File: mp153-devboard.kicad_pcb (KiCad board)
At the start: 4 copper layers, 39.9 x 57.9 mm, 117 parts, among them CON1 microSDCon_SMT_104031-0811, J1 Pins_02x04_RightAngle_P2.54mm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, J2 Pins_02x05_P1.27mm_SMT, J3 USB-C_Receptacle_Molex_217179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, J4 Pins_02x40_P0.4mm_W3.0mm_SMT, J5 Conn_01x02, J6 Pins_02x40_P0.4mm_W3.0mm_SMT, U13 NCP51460SN33, U14 DDR3L-RAM-4Gb_MT41K256M16TW, U15 AP6230xZ6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

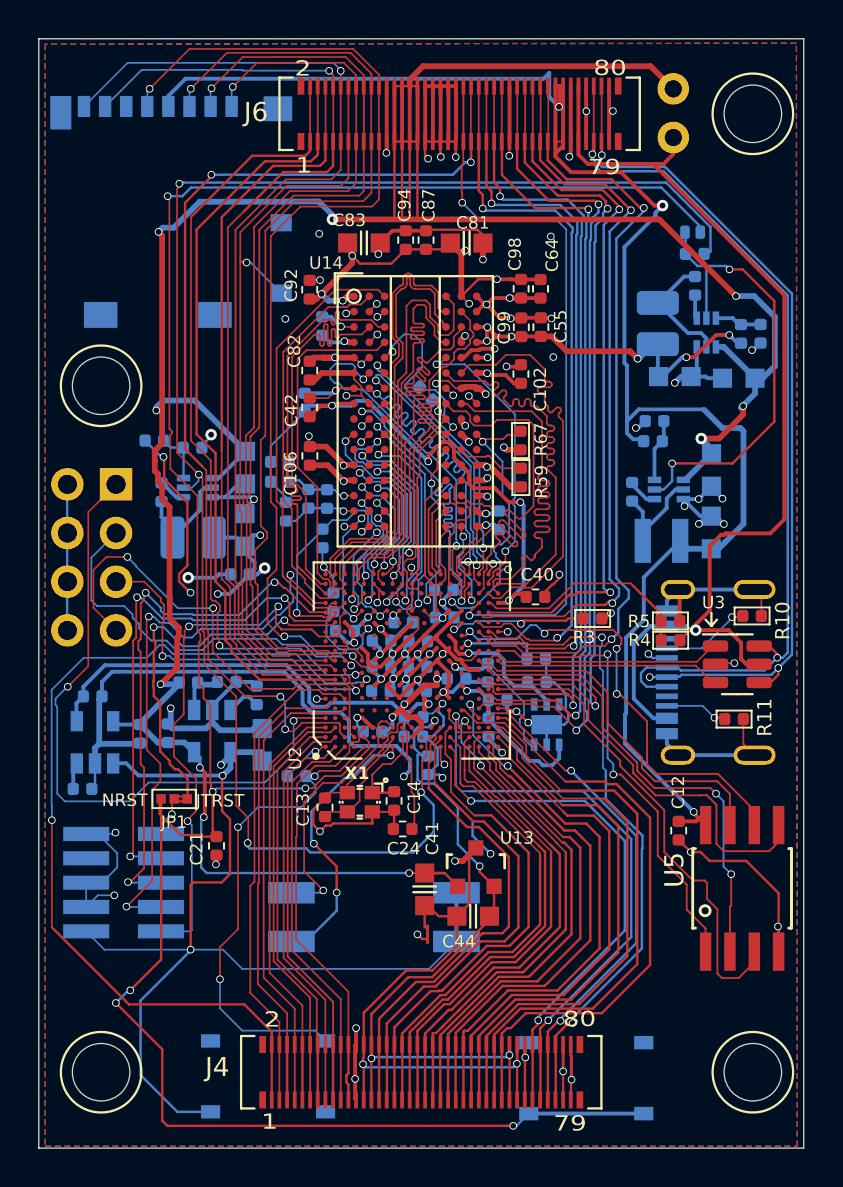
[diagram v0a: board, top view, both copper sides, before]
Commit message: p2 carrier board: fixed position of headers
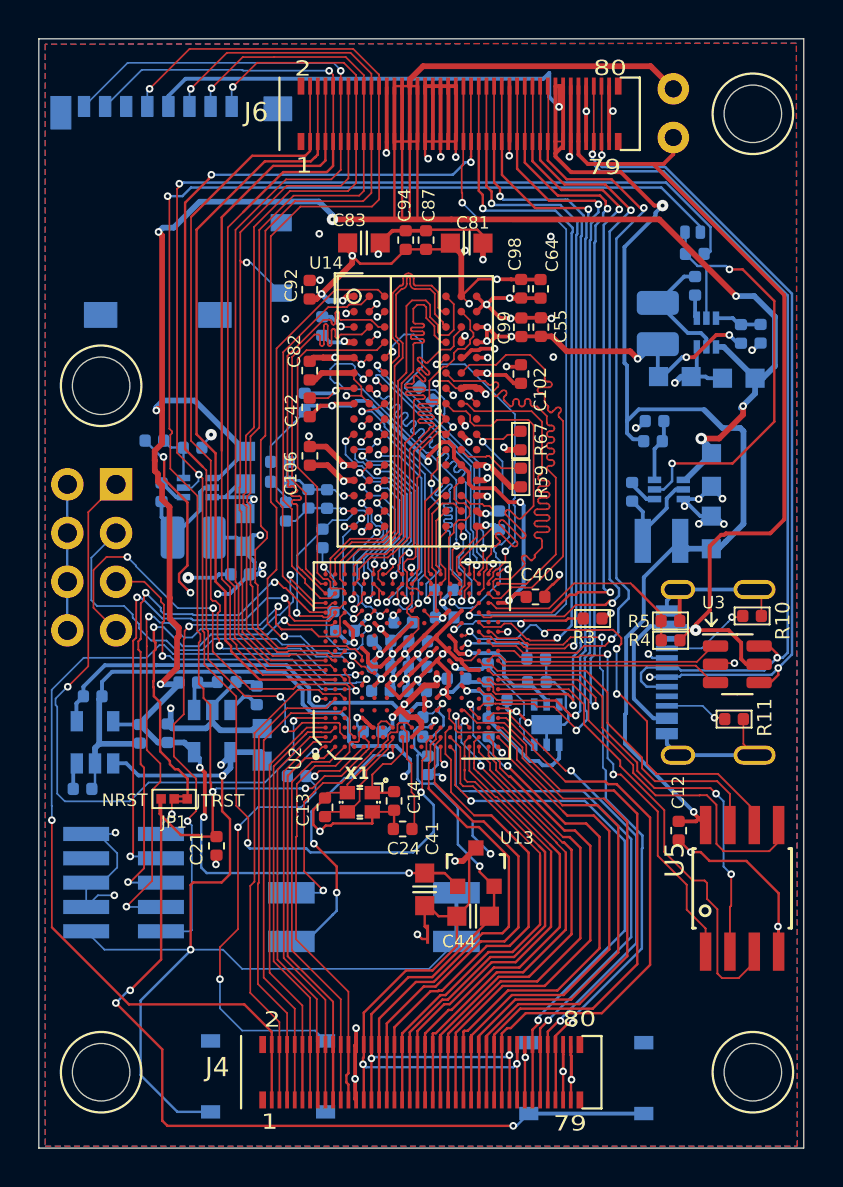
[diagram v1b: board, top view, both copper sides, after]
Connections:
- net /D14 renamed /I2C2_SDA
- net /D25 renamed /I2C2_SCL
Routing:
- net VDD_DDR: track 78.0 -> 64.5 mm
- net VDD_CORE: track 32.6 -> 32.9 mm, vias 10 -> 11

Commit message: devboard v0.1: rename all header pins
No electrical changes made: only renamed pins to use PX# style (e.g. "PA0") instead of D# style (e.g. "D23")
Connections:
- net /ADC-10 renamed /PC0
- net /ADC-11 renamed /PC1
- net /ADC-12 renamed /PC2
- net /ADC-13 renamed /PC3
- net /ADC-14 renamed /PA2
- net /ADC-15 renamed /PA3
- net /ADC-16 renamed /PA0
- net /ADC-17 renamed /PA1
- net /ADC-18_DAC0 renamed /PA4
- net /ADC-19_DAC1 renamed /PA5
- net /ADC-2 renamed /PF11
- net /ADC-3 renamed /PA6
- net /ADC-4 renamed /PC4
- net /ADC-5 renamed /PB1
- net /ADC-7 renamed /PA7
- net /ADC-8 renamed /PC5
- net /ADC-9 renamed /PB0
- net /D0 renamed /PA9
- net /D1 renamed /PE13
- net /D10 renamed /PA8
- net /D11 renamed /PE10
- net /D12 renamed /PE4
- net /D13 renamed /PD1
- net /D15 renamed /PD0
- net /D16 renamed /PC8
- net /D17 renamed /PC9
- net /D18 renamed /PC10
- net /D19 renamed /PC11
- net /D2 renamed /PB7
- net /D20 renamed /PE12
- net /D21 renamed /PA12
- net /D22 renamed /PB15
- net /D23 renamed /PB14
- net /D24 renamed /PG9
- net /D26 renamed /PB8
- net /D27 renamed /PG13
- net /D28 renamed /PE3
- net /D29 renamed /PE2
- net /D3 renamed /PB4
- net /D30 renamed /PB2
- net /D4 renamed /PD2
- net /D5 renamed /PA11
- net /D6 renamed /PB10
- net /D7 renamed /PA10
- net /D8 renamed /PE6
- net /D9 renamed /PC12
- net /I2C2_SCL renamed /PD7
- net /I2C2_SDA renamed /PG15
- net /SAI_FS renamed /PD12
- net /SAI_MCLK renamed /PE0
- net /SAI_SCK renamed /PD13
- net /SAI_SD_A renamed /PD11
- net /SAI_SD_B renamed /PG10
